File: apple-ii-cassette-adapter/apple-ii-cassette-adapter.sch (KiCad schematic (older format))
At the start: 20 parts, among them J1 LCD_I2C, J2 POWER, J3 ADAFRUIT_SDCARD, J4 AUDIO, J5 AUDIO, J6 BUTTONS, SW1 PLAY, SW2 STOP, SW3 PREV, SW4 NEXT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

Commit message: Update title!
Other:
- note added: "Adrian Chadd <adrian@freebsd.org>"
- note added: "Apple ii cassette player - prototype 2"
- note added: "September 1, 2021"

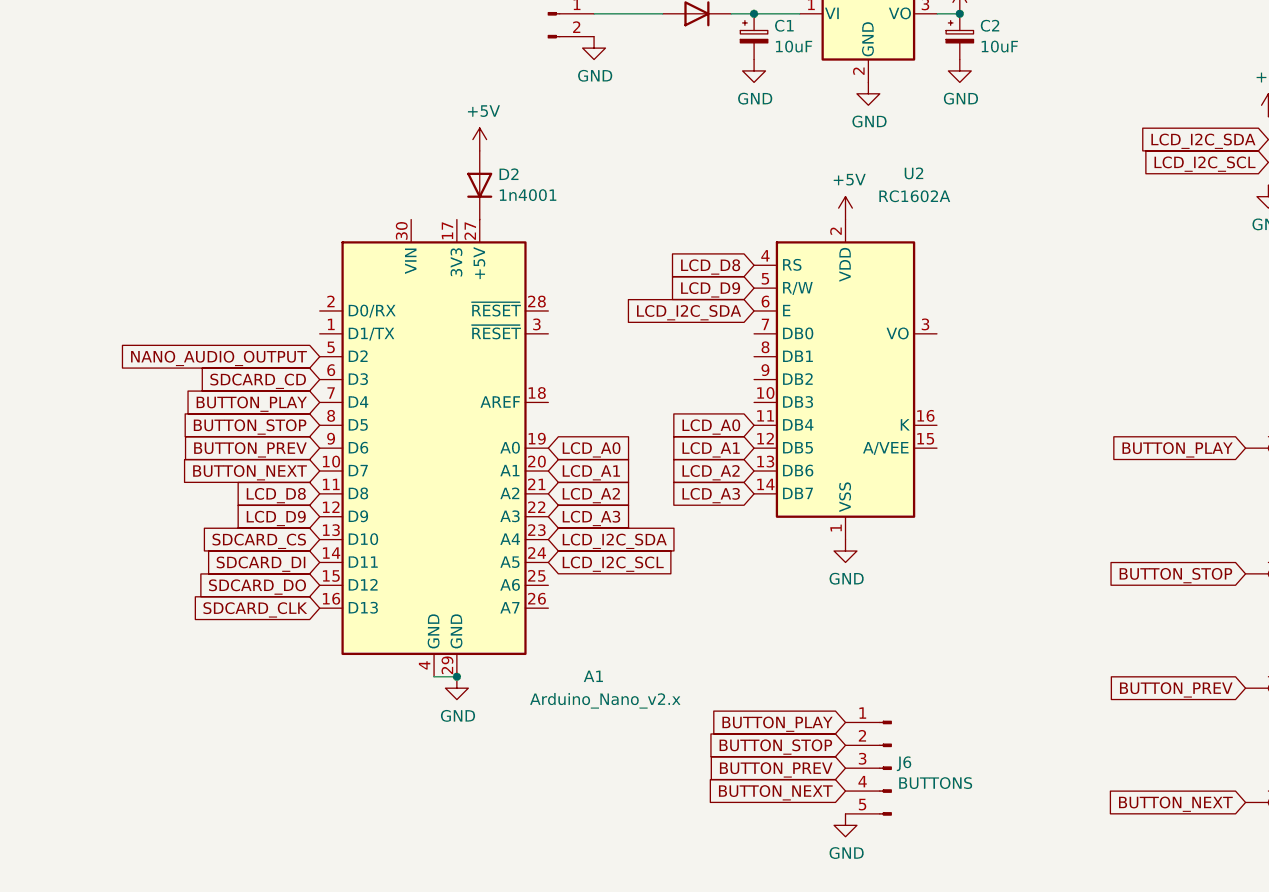
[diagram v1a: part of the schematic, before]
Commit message: Update schematic to aid in layout, start layout
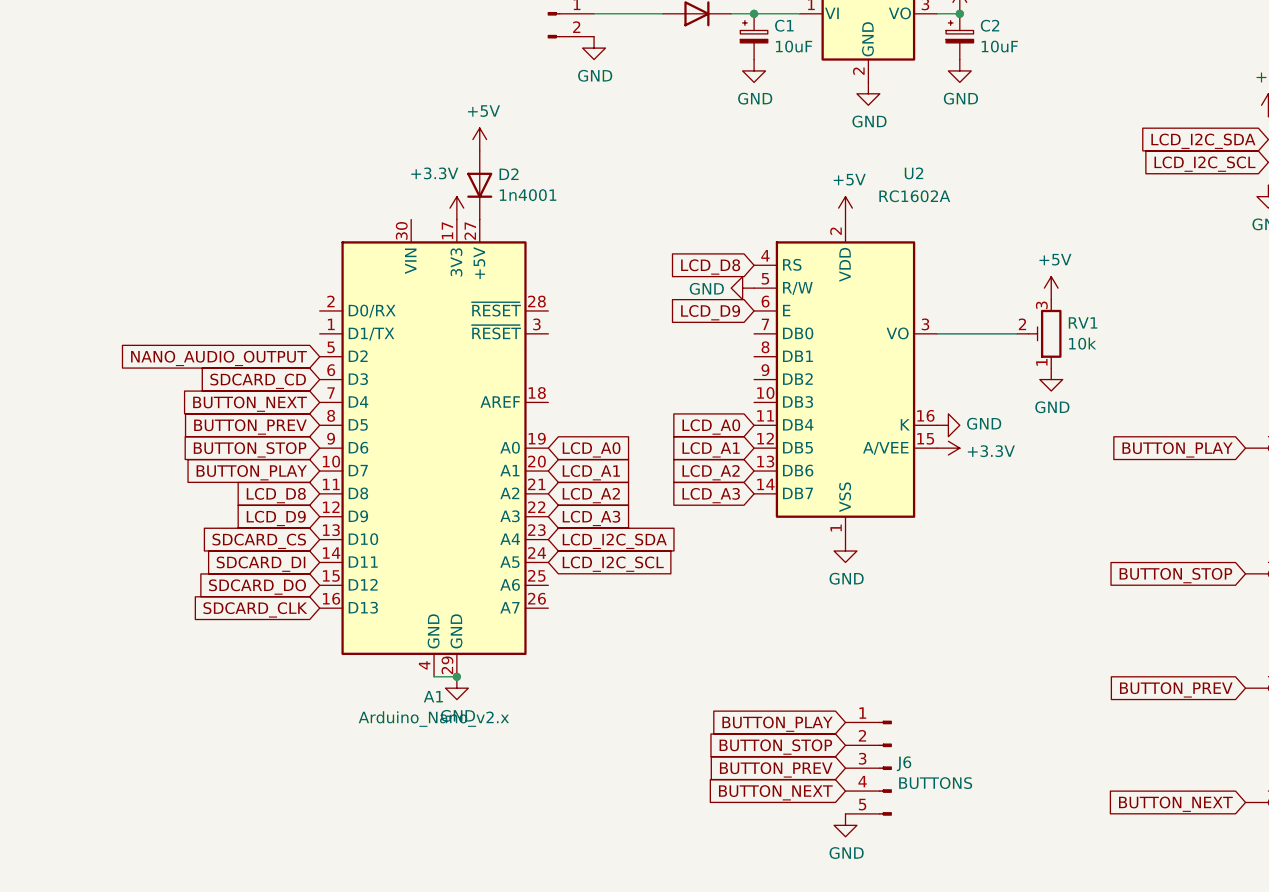
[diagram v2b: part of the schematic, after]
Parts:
- added RV1: 10k, Potentiometer_THT:Potentiometer_Bourns_3266P_Horizontal, symbol Device:R_POT_TRIM
- C1, C2, C3: footprint (none) -> Capacitor_THT:CP_Radial_D6.3mm_P2.50mm
- D1, D2: footprint (none) -> Diode_THT:D_DO-15_P10.16mm_Horizontal
- J1: footprint (none) -> Connector_PinHeader_2.54mm:PinHeader_1x04_P2.54mm_Vertical
- J2, J5: footprint (none) -> Connector_PinHeader_2.54mm:PinHeader_1x02_P2.54mm_Vertical
- J3: footprint (none) -> Connector_PinHeader_2.54mm:PinHeader_1x08_P2.54mm_Vertical
- J4: footprint (none) -> Connector_Audio:Jack_3.5mm_Ledino_KB3SPRS_Horizontal
- J6: footprint (none) -> Connector_PinHeader_2.54mm:PinHeader_1x05_P2.54mm_Vertical
- R1, R2: footprint (none) -> Resistor_THT:R_Axial_DIN0207_L6.3mm_D2.5mm_P2.54mm_Vertical
- SW1, SW2, SW3, SW4: footprint (none) -> Button_Switch_THT:KSA_Tactile_SPST
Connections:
- net +5V: now also RV1.3
- net BUTTON_NEXT: now also A1.7 (D4); no longer A1.10 (D7)
- net BUTTON_PLAY: now also A1.10 (D7); no longer A1.7 (D4)
- net BUTTON_PREV: now also A1.8 (D5); no longer A1.9 (D6)
- net BUTTON_STOP: now also A1.9 (D6); no longer A1.8 (D5)
- net GND: now also U2.16 (K), U2.5 (R/W), RV1.1
- net LCD_D9: now also U2.6 (E); no longer U2.5 (R/W)
- net LCD_I2C_SDA: no longer U2.6 (E)
- net +3V3: now reaches A1.17 (3V3)
- net +3V3: now also U2.15 (A/VEE)
- net at U2.3 (VO): now also RV1.2

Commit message: In progress schematic layout
For some reason I don't have a ground pin on this audio jack footprint; i need
to figure THAT out soon.
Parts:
- added J8: DC Input, Connector_BarrelJack:BarrelJack_CUI_PJ-102AH_Horizontal, symbol Connector:Barrel_Jack_Switch
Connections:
- net GND: now also J4.G, J8.2
- net LCD_D8: now also U2.6 (E); no longer U2.4 (RS)
- net LCD_D9: now also U2.4 (RS); no longer U2.6 (E)
- net PWR_IN: now reaches D1.2 (A), J2.1 (Pin_1)
- net PWR_IN: now also J8.1
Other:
- moved on the sheet: J2
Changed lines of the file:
@@
 L power:GND #PWR0115
 U 1 1 6130002D
-P 3100 1200
-F 0 "#PWR0115" H 3100 950 50  0001 C CNN
-F 1 "GND" H 3105 1027 50  0000 C CNN
-F 2 "" H 3100 1200 50  0001 C CNN
-F 3 "" H 3100 1200 50  0001 C CNN
-	1    3100 1200
+P 1500 1700
+F 0 "#PWR0115" H 1500 1450 50  0001 C CNN
+F 1 "GND" H 1505 1527 50  0000 C CNN
+F 2 "" H 1500 1700 50  0001 C CNN
+F 3 "" H 1500 1700 50  0001 C CNN
+	1    1500 1700
 	1    0    0    -1
 $EndComp
@@
 L Connector:Conn_01x02_Male J2
 U 1 1 612FCFD9
-P 2900 1100
-F 0 "J2" H 3008 1281 50  0000 C CNN
-F 1 "POWER" H 3008 1190 50  0000 C CNN
-F 2 "Connector_PinHeader_2.54mm:PinHeader_1x02_P2.54mm_Vertical" H 2900 1100 50  0001 C CNN
-F 3 "~" H 2900 1100 50  0001 C CNN
-	1    2900 1100
+P 1300 1600
+F 0 "J2" H 1408 1781 50  0000 C CNN
+F 1 "POWER" H 1408 1690 50  0000 C CNN
+F 2 "Connector_PinHeader_2.54mm:PinHeader_1x02_P2.54mm_Vertical" H 1300 1600 50  0001 C CNN
+F 3 "~" H 1300 1600 50  0001 C CNN
+	1    1300 1600
 	1    0    0    -1
 $EndComp
@@
 Text GLabel 1900 2700 0    50   Input ~ 0
 SDCARD_CD
+Text GLabel 3800 2200 0    50   Input ~ 0
+LCD_D9
 Text GLabel 3800 2400 0    50   Input ~ 0
-LCD_D9
-Text GLabel 3800 2200 0    50   Input ~ 0
 LCD_D8
 Text GLabel 3800 3200 0    50   Input ~ 0
@@
 $EndComp
 Connection ~ 2500 4000
+$Comp
+L power:GND #PWR0124
+U 1 1 613AA1CD
+P 1450 1100
+F 0 "#PWR0124" H 1450 850 50  0001 C CNN
+F 1 "GND" H 1455 927 50  0000 C CNN
+F 2 "" H 1450 1100 50  0001 C CNN
+F 3 "" H 1450 1100 50  0001 C CNN
+	1    1450 1100
+	1    0    0    -1
+$EndComp
+Text GLabel 3100 1100 0    50   Input ~ 0
+PWR_IN
+Text GLabel 1450 900  2    50   Input ~ 0
+PWR_IN
+Text GLabel 1500 1600 2    50   Input ~ 0
+PWR_IN
+$Comp
+L Connector:Barrel_Jack_Switch J8
+U 1 1 613B2A75
+P 1150 1000
+F 0 "J8" H 1207 1317 50  0000 C CNN
+F 1 "DC Input" H 1207 1226 50  0000 C CNN
+F 2 "Connector_BarrelJack:BarrelJack_CUI_PJ-102AH_Horizontal" H 1200 960 50  0001 C CNN
+F 3 "~" H 1200 960 50  0001 C CNN
+	1    1150 1000
+	1    0    0    -1
+$EndComp
+$Comp
+L power:GND #PWR?
+U 1 1 613D2A20
+P 2800 6200
+F 0 "#PWR?" H 2800 5950 50  0001 C CNN
+F 1 "GND" H 2805 6027 50  0000 C CNN
+F 2 "" H 2800 6200 50  0001 C CNN
+F 3 "" H 2800 6200 50  0001 C CNN
+	1    2800 6200
+	1    0    0    -1
+$EndComp
 $EndSCHEMATC

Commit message: Update schematic/PCB; this may actually work.
"S" is the shield; not GND. Weird. Anyway, that's GND now.
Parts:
- removed J4: AUDIO, Connector_Audio:Jack_3.5mm_Ledino_KB3SPRS_Horizontal, symbol Connector:AudioJack2_Ground_Switch
- added J4: AUDIO, Connector_Audio:Jack_3.5mm_Ledino_KB3SPRS_Horizontal, symbol Connector:AudioJack3_Ground_SwitchTR
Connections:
- net AUDIO_OUT: now also J4.T
- net GND: now also J4.S
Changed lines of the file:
@@
 NANO_AUDIO_OUTPUT
-$Comp
-L Connector:AudioJack2_Ground_Switch J4
-U 1 1 6132D793
-P 2800 5900
-F 0 "J4" H 2832 6325 50  0000 C CNN
-F 1 "AUDIO" H 2832 6234 50  0000 C CNN
-F 2 "Connector_Audio:Jack_3.5mm_Ledino_KB3SPRS_Horizontal" H 2800 6100 50  0001 C CNN
-F 3 "~" H 2800 6100 50  0001 C CNN
-	1    2800 5900
-	1    0    0    -1
-$EndComp
 $Comp
 L Connector:Conn_01x02_Male J5
@@
 $EndComp
 $Comp
-L power:GND #PWR?
-U 1 1 613D2A20
-P 2800 6200
-F 0 "#PWR?" H 2800 5950 50  0001 C CNN
-F 1 "GND" H 2805 6027 50  0000 C CNN
-F 2 "" H 2800 6200 50  0001 C CNN
-F 3 "" H 2800 6200 50  0001 C CNN
-	1    2800 6200
-	1    0    0    -1
+L Connector:AudioJack3_Ground_SwitchTR J4
+U 1 1 613EAD6A
+P 2800 5700
+F 0 "J4" H 2782 6025 50  0000 C CNN
+F 1 "AUDIO" H 2782 5934 50  0000 C CNN
+F 2 "Connector_Audio:Jack_3.5mm_Ledino_KB3SPRS_Horizontal" H 2800 5700 50  0001 C CNN
+F 3 "~" H 2800 5700 50  0001 C CNN
+	1    2800 5700
+	1    0    0    -1
+$EndComp
+$Comp
+L power:GND #PWR0126
+U 1 1 613F1F0F
+P 3000 5600
+F 0 "#PWR0126" H 3000 5350 50  0001 C CNN
+F 1 "GND" H 3005 5427 50  0000 C CNN
+F 2 "" H 3000 5600 50  0001 C CNN
+F 3 "" H 3000 5600 50  0001 C CNN
+	1    3000 5600
+	0    -1   -1   0
 $EndComp
 $EndSCHEMATC

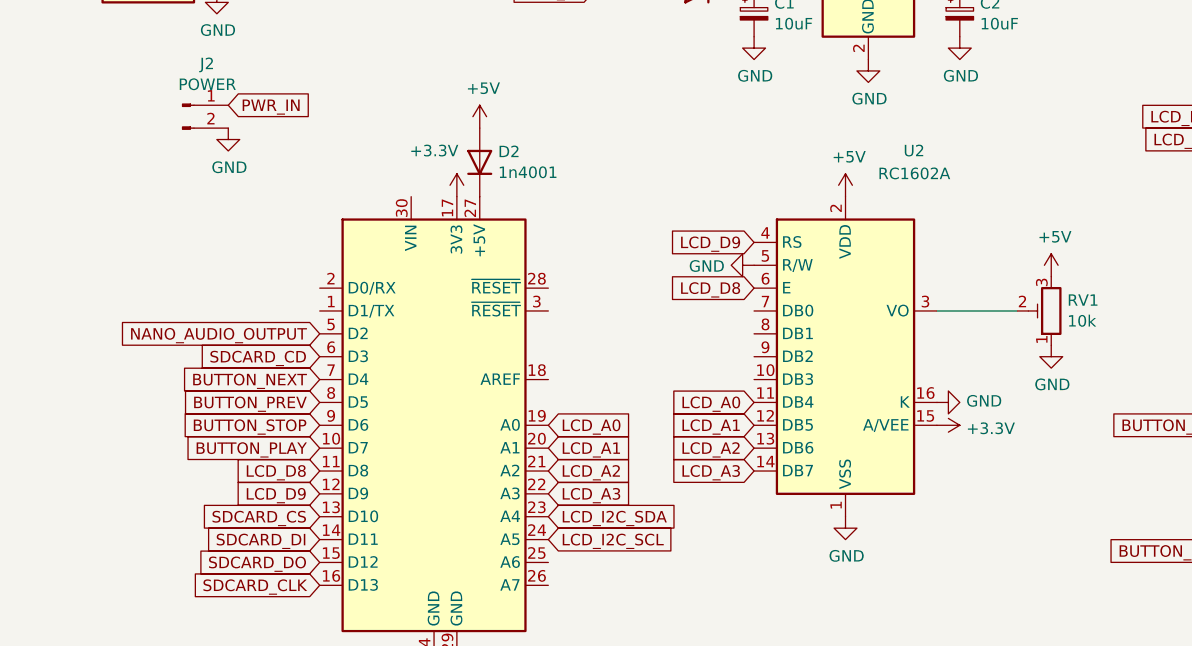
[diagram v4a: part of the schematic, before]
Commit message: Update routing and schematic for the RC1602A LCD variant.
It's not the adafruit one, and honestly I'm suprised kicad doesn't come with
the adafruit part footprints, but baby steps.
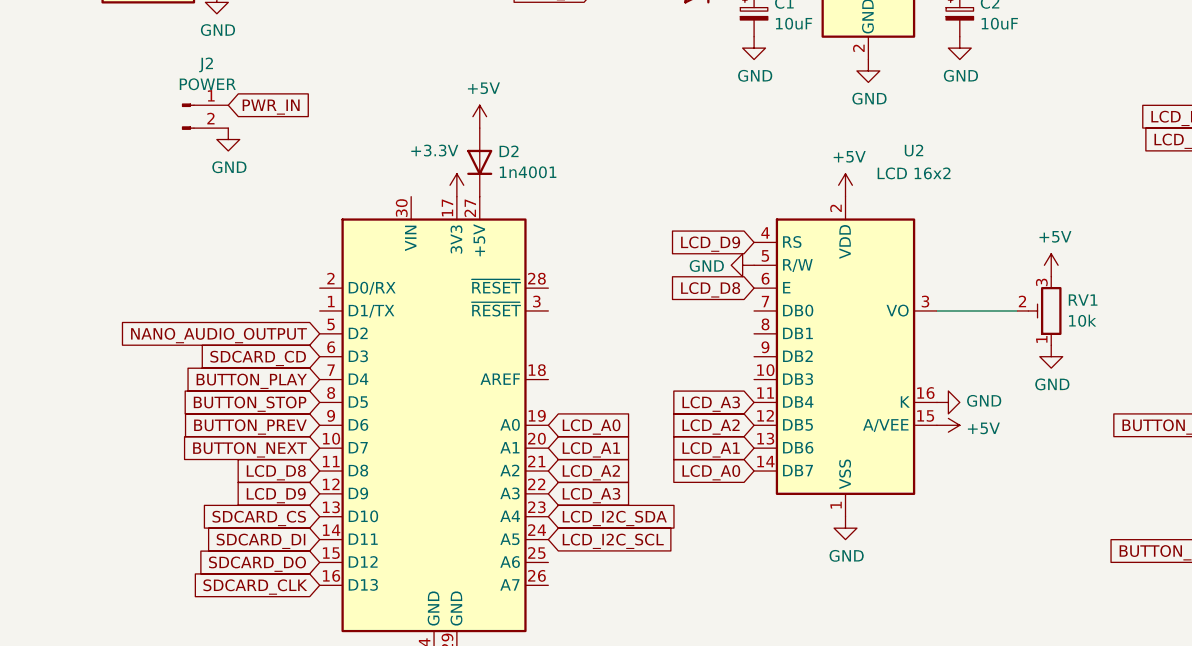
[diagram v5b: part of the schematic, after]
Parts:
- U2: value RC1602A -> LCD 16x2
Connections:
- net +3V3: no longer U2.15 (A/VEE)
- net +5V: now also U2.15 (A/VEE)
- net BUTTON_NEXT: now also A1.10 (D7); no longer A1.7 (D4)
- net BUTTON_PLAY: now also A1.7 (D4); no longer A1.10 (D7)
- net BUTTON_PREV: now also A1.9 (D6); no longer A1.8 (D5)
- net BUTTON_STOP: now also A1.8 (D5); no longer A1.9 (D6)
- net LCD_A0: now also U2.14 (DB7); no longer U2.11 (DB4)
- net LCD_A1: now also U2.13 (DB6); no longer U2.12 (DB5)
- net LCD_A2: now also U2.12 (DB5); no longer U2.13 (DB6)
- net LCD_A3: now also U2.11 (DB4); no longer U2.14 (DB7)
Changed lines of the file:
@@
 Text GLabel 1900 3200 0    50   Input ~ 0
 LCD_D8
+Text GLabel 1900 3100 0    50   Input ~ 0
+BUTTON_NEXT
+Text GLabel 1900 3000 0    50   Input ~ 0
+BUTTON_PREV
+Text GLabel 1900 2900 0    50   Input ~ 0
+BUTTON_STOP
 Text GLabel 1900 2800 0    50   Input ~ 0
-BUTTON_NEXT
-Text GLabel 1900 2900 0    50   Input ~ 0
-BUTTON_PREV
-Text GLabel 1900 3000 0    50   Input ~ 0
-BUTTON_STOP
-Text GLabel 1900 3100 0    50   Input ~ 0
 BUTTON_PLAY
 Text GLabel 2900 3300 2    50   Input ~ 0
@@
 Text GLabel 3800 2400 0    50   Input ~ 0
 LCD_D8
+Text GLabel 3800 2900 0    50   Input ~ 0
+LCD_A3
+Text GLabel 3800 3000 0    50   Input ~ 0
+LCD_A2
+Text GLabel 3800 3100 0    50   Input ~ 0
+LCD_A1
 Text GLabel 3800 3200 0    50   Input ~ 0
-LCD_A3
-Text GLabel 3800 3100 0    50   Input ~ 0
-LCD_A2
-Text GLabel 3800 3000 0    50   Input ~ 0
-LCD_A1
-Text GLabel 3800 2900 0    50   Input ~ 0
 LCD_A0
 $Comp
@@
 P 4200 2700
 F 0 "U2" H 4500 3600 50  0000 C CNN
-F 1 "RC1602A" H 4500 3500 50  0000 C CNN
+F 1 "LCD 16x2" H 4500 3500 50  0000 C CNN
 F 2 "Display:RC1602A" H 4300 1900 50  0001 C CNN
 F 3 "http://www.raystar-optronics.com/down.php?ProID=18" H 4300 2600 50  0001 C CNN
@@
 $EndComp
 $Comp
+L power:GND #PWR0123
+U 1 1 6134279C
+P 3800 2300
+F 0 "#PWR0123" H 3800 2050 50  0001 C CNN
+F 1 "GND" V 3805 2172 50  0000 R CNN
+F 2 "" H 3800 2300 50  0001 C CNN
+F 3 "" H 3800 2300 50  0001 C CNN
+	1    3800 2300
+	0    1    1    0
+$EndComp
+Text GLabel 1900 3300 0    50   Input ~ 0
+LCD_D9
+$Comp
+L MCU_Module:Arduino_Nano_v2.x A1
+U 1 1 6138AAE6
+P 2400 3000
+F 0 "A1" H 2400 1911 50  0000 C CNN
+F 1 "Arduino_Nano_v2.x" H 2400 1820 50  0000 C CNN
+F 2 "Module:Arduino_Nano" H 2400 3000 50  0001 C CIN
+F 3 "https://www.arduino.cc/en/uploads/Main/ArduinoNanoManual23.pdf" H 2400 3000 50  0001 C CNN
+	1    2400 3000
+	1    0    0    -1
+$EndComp
+Connection ~ 2500 4000
+$Comp
+L power:GND #PWR0124
+U 1 1 613AA1CD
+P 1450 1100
+F 0 "#PWR0124" H 1450 850 50  0001 C CNN
+F 1 "GND" H 1455 927 50  0000 C CNN
+F 2 "" H 1450 1100 50  0001 C CNN
+F 3 "" H 1450 1100 50  0001 C CNN
+	1    1450 1100
+	1    0    0    -1
+$EndComp
+Text GLabel 3100 1100 0    50   Input ~ 0
+PWR_IN
+Text GLabel 1450 900  2    50   Input ~ 0
+PWR_IN
+Text GLabel 1500 1600 2    50   Input ~ 0
+PWR_IN
+$Comp
+L Connector:Barrel_Jack_Switch J8
+U 1 1 613B2A75
+P 1150 1000
+F 0 "J8" H 1207 1317 50  0000 C CNN
+F 1 "DC Input" H 1207 1226 50  0000 C CNN
+F 2 "Connector_BarrelJack:BarrelJack_CUI_PJ-102AH_Horizontal" H 1200 960 50  0001 C CNN
+F 3 "~" H 1200 960 50  0001 C CNN
+	1    1150 1000
+	1    0    0    -1
+$EndComp
+$Comp
+L Connector:AudioJack3_Ground_SwitchTR J4
+U 1 1 613EAD6A
+P 2800 5700
+F 0 "J4" H 2782 6025 50  0000 C CNN
+F 1 "AUDIO" H 2782 5934 50  0000 C CNN
+F 2 "Connector_Audio:Jack_3.5mm_Ledino_KB3SPRS_Horizontal" H 2800 5700 50  0001 C CNN
+F 3 "~" H 2800 5700 50  0001 C CNN
+	1    2800 5700
+	1    0    0    -1
+$EndComp
+$Comp
+L power:GND #PWR0126
+U 1 1 613F1F0F
+P 3000 5600
+F 0 "#PWR0126" H 3000 5350 50  0001 C CNN
+F 1 "GND" H 3005 5427 50  0000 C CNN
+F 2 "" H 3000 5600 50  0001 C CNN
+F 3 "" H 3000 5600 50  0001 C CNN
+	1    3000 5600
+	0    -1   -1   0
+$EndComp
+$Comp
+L power:+5V #PWR0122
+U 1 1 6132EB5A
+P 5100 2350
+F 0 "#PWR0122" H 5100 2200 50  0001 C CNN
+F 1 "+5V" H 5115 2523 50  0000 C CNN
+F 2 "" H 5100 2350 50  0001 C CNN
+F 3 "" H 5100 2350 50  0001 C CNN
+	1    5100 2350
+	1    0    0    -1
+$EndComp
+$Comp
+L power:GND #PWR0121
+U 1 1 6132E60D
+P 5100 2650
+F 0 "#PWR0121" H 5100 2400 50  0001 C CNN
+F 1 "GND" H 5105 2477 50  0000 C CNN
+F 2 "" H 5100 2650 50  0001 C CNN
+F 3 "" H 5100 2650 50  0001 C CNN
+	1    5100 2650
+	1    0    0    -1
+$EndComp
+Wire Wire Line
+	4950 2500 4600 2500
+$Comp
+L Device:R_POT_TRIM RV1
+U 1 1 6132C818
+P 5100 2500
+F 0 "RV1" H 5030 2454 50  0000 R CNN
+F 1 "10k" H 5030 2545 50  0000 R CNN
+F 2 "Potentiometer_THT:Potentiometer_Bourns_3266P_Horizontal" H 5100 2500 50  0001 C CNN
+F 3 "~" H 5100 2500 50  0001 C CNN
+	1    5100 2500
+	-1   0    0    1
+$EndComp
+$Comp
 L power:GND #PWR0119
 U 1 1 6132B40F
@@
 $EndComp
 $Comp
-L power:+3.3V #PWR0120
-U 1 1 6132BB37
+L power:+5V #PWR0120
+U 1 1 614C7FA0
 P 4600 3000
 F 0 "#PWR0120" H 4600 2850 50  0001 C CNN
-F 1 "+3.3V" V 4615 3128 50  0000 L CNN
+F 1 "+5V" V 4615 3128 50  0000 L CNN
 F 2 "" H 4600 3000 50  0001 C CNN
 F 3 "" H 4600 3000 50  0001 C CNN
@@
 	0    1    1    0
 $EndComp
-$Comp
-L Device:R_POT_TRIM RV1
-U 1 1 6132C818
-P 5100 2500
-F 0 "RV1" H 5030 2454 50  0000 R CNN
-F 1 "10k" H 5030 2545 50  0000 R CNN
-F 2 "Potentiometer_THT:Potentiometer_Bourns_3266P_Horizontal" H 5100 2500 50  0001 C CNN
-F 3 "~" H 5100 2500 50  0001 C CNN
-	1    5100 2500
-	-1   0    0    1
-$EndComp
-Wire Wire Line
-	4950 2500 4600 2500
-$Comp
-L power:GND #PWR0121
-U 1 1 6132E60D
-P 5100 2650
-F 0 "#PWR0121" H 5100 2400 50  0001 C CNN
-F 1 "GND" H 5105 2477 50  0000 C CNN
-F 2 "" H 5100 2650 50  0001 C CNN
-F 3 "" H 5100 2650 50  0001 C CNN
-	1    5100 2650
-	1    0    0    -1
-$EndComp
-$Comp
-L power:+5V #PWR0122
-U 1 1 6132EB5A
-P 5100 2350
-F 0 "#PWR0122" H 5100 2200 50  0001 C CNN
-F 1 "+5V" H 5115 2523 50  0000 C CNN
-F 2 "" H 5100 2350 50  0001 C CNN
-F 3 "" H 5100 2350 50  0001 C CNN
-	1    5100 2350
-	1    0    0    -1
-$EndComp
-$Comp
-L power:GND #PWR0123
-U 1 1 6134279C
-P 3800 2300
-F 0 "#PWR0123" H 3800 2050 50  0001 C CNN
-F 1 "GND" V 3805 2172 50  0000 R CNN
-F 2 "" H 3800 2300 50  0001 C CNN
-F 3 "" H 3800 2300 50  0001 C CNN
-	1    3800 2300
-	0    1    1    0
-$EndComp
-Text GLabel 1900 3300 0    50   Input ~ 0
-LCD_D9
-$Comp
-L MCU_Module:Arduino_Nano_v2.x A1
-U 1 1 6138AAE6
-P 2400 3000
-F 0 "A1" H 2400 1911 50  0000 C CNN
-F 1 "Arduino_Nano_v2.x" H 2400 1820 50  0000 C CNN
-F 2 "Module:Arduino_Nano" H 2400 3000 50  0001 C CIN
-F 3 "https://www.arduino.cc/en/uploads/Main/ArduinoNanoManual23.pdf" H 2400 3000 50  0001 C CNN
-	1    2400 3000
-	1    0    0    -1
-$EndComp
-Connection ~ 2500 4000
-$Comp
-L power:GND #PWR0124
-U 1 1 613AA1CD
-P 1450 1100
-F 0 "#PWR0124" H 1450 850 50  0001 C CNN
-F 1 "GND" H 1455 927 50  0000 C CNN
-F 2 "" H 1450 1100 50  0001 C CNN
-F 3 "" H 1450 1100 50  0001 C CNN
-	1    1450 1100
-	1    0    0    -1
-$EndComp
-Text GLabel 3100 1100 0    50   Input ~ 0
-PWR_IN
-Text GLabel 1450 900  2    50   Input ~ 0
-PWR_IN
-Text GLabel 1500 1600 2    50   Input ~ 0
-PWR_IN
-$Comp
-L Connector:Barrel_Jack_Switch J8
-U 1 1 613B2A75
-P 1150 1000
-F 0 "J8" H 1207 1317 50  0000 C CNN
-F 1 "DC Input" H 1207 1226 50  0000 C CNN
-F 2 "Connector_BarrelJack:BarrelJack_CUI_PJ-102AH_Horizontal" H 1200 960 50  0001 C CNN
-F 3 "~" H 1200 960 50  0001 C CNN
-	1    1150 1000
-	1    0    0    -1
-$EndComp
-$Comp
-L Connector:AudioJack3_Ground_SwitchTR J4
-U 1 1 613EAD6A
-P 2800 5700
-F 0 "J4" H 2782 6025 50  0000 C CNN
-F 1 "AUDIO" H 2782 5934 50  0000 C CNN
-F 2 "Connector_Audio:Jack_3.5mm_Ledino_KB3SPRS_Horizontal" H 2800 5700 50  0001 C CNN
-F 3 "~" H 2800 5700 50  0001 C CNN
-	1    2800 5700
-	1    0    0    -1
-$EndComp
-$Comp
-L power:GND #PWR0126
-U 1 1 613F1F0F
-P 3000 5600
-F 0 "#PWR0126" H 3000 5350 50  0001 C CNN
-F 1 "GND" H 3005 5427 50  0000 C CNN
-F 2 "" H 3000 5600 50  0001 C CNN
-F 3 "" H 3000 5600 50  0001 C CNN
-	1    3000 5600
-	0    -1   -1   0
-$EndComp
 $EndSCHEMATC
